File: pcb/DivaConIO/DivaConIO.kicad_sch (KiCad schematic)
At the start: 59 parts, among them J1 Conn_01x06_MountingPin, J2 Conn_01x04_MountingPin, J3 Conn_01x06_MountingPin, J4 Conn_01x08_MountingPin, J5 JST_SH_BM03B-SRSS-TB, J6 Conn_01x05_MountingPin, J7 Conn_01x06_MountingPin, Q1 BSS138, Q2 BSS138, Q3 BSS138, Q4 BSS138, Q5 BSS138, SW1 SW_Push

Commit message: revision 1.0 pcb schematics and layout
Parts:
- removed C5, C6: 1u0, Capacitor_SMD:C_0603_1608Metric, symbol Device:C_Small
- removed Q1: BSS138, Package_TO_SOT_SMD:SOT-23, symbol Transistor_FET:BSS138
- added C7: 100n, Capacitor_SMD:C_0603_1608Metric, symbol Device:C_Small
- added FID1, FID2, FID3, FID4: Fiducial, Fiducial:Fiducial_0.5mm_Mask1.5mm, symbol Mechanical:Fiducial
- added TP1, TP10, TP11, TP12, TP2, TP3, TP4, TP5, TP6, TP7, TP8, TP9: TestPoint, TestPoint:TestPoint_Pad_D2.0mm, symbol Connector:TestPoint
- added U1: 74HCT1G14, Package_TO_SOT_SMD:SC-74A-5_1.55x2.9mm_P0.95mm, symbol 74xGxx:74AHCT1G14
- J1, J3, J7: value Conn_01x06_MountingPin -> B6B-PH-SM4-TBT
- J2: value Conn_01x04_MountingPin -> B4B-PH-SM4-TBT
- J4: value Conn_01x08_MountingPin -> B8B-PH-SM4-TBT
- J5: value JST_SH_BM03B-SRSS-TB -> BM03B-SRSS-TBT
- R18: value 4K7 -> 330R
- R19: value 10R -> 10K
- SW1: footprint Button_Switch_SMD:SW_Push_SPST_NO_Alps_SKRK -> DivaConIO:SW_Push_SPST_NO_Alps_SKRP
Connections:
- net +3V3: now also TP1.1
- net +5V: now also C7.1, TP2.1, U1.5 (VCC); no longer R18.1
- net Display_I2C0_SCL: now also TP8.1
- net Display_I2C0_SDA: now also TP7.1
- net GND: now also R19.2, C7.2, TP10.1, TP4.1, U1.3 (GND)
- net Slider_I2C1_SCL: now also R13.2, TP5.1; no longer R15.2
- net Slider_I2C1_SDA: now also J4.4 (Pin_4), R15.2, TP6.1; no longer J4.6 (Pin_6), R13.2
- net Slider_LED_Data: now also U1.2
- net at R18.2: now also J4.6 (Pin_6), TP3.1; no longer J4.4 (Pin_4)
- net at J5.1 (Pin_1): now also A1.D1 (SWCLK), TP11.1; no longer A1.D3 (SWDIO)
- net at J5.3 (Pin_3): now also A1.D3 (SWDIO), TP12.1; no longer A1.D1 (SWCLK)
- net at A1.30 (RUN), R20.2, SW1.2: now also TP9.1
- net LED_Circle renamed LED-_Circle
- net LED_Cross renamed LED-_Cross
- net LED_Square renamed LED-_Square
- net LED_Triangle renamed LED-_Triangle
- new net: R18.1, U1.4
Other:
- moved on the sheet: J4, J5, R13, R15, R16, R17, R20, SW1

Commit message: revision 1.1 pcb schematics and layout
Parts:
- removed R23: 10R, Resistor_SMD:R_0603_1608Metric, symbol Device:R
- removed R26: 330R, Resistor_SMD:R_0603_1608Metric, symbol Device:R
- added R20: 10R, Resistor_SMD:R_0603_1608Metric, symbol Device:R
- added R32: 330R, Resistor_SMD:R_0603_1608Metric, symbol Device:R
- renumbered C7 to C5, FID3 to FID2, FID2 to FID3, J6 to J4, J4 to J6, Q5 to Q1, Q4 to Q2, Q2 to Q4, R9 to R10, R31 to R11, R10 to R12, R30 to R13, R11 to R14, R29 to R15, R12 to R16, R14 to R17, R20 to R18, R24 to R19, R19 to R23, R28 to R24, R18 to R26, R17 to R28, R16 to R29, R15 to R30, R13 to R31, R32 to R9, TP12 to TP1, TP5 to TP10, TP3 to TP11, TP10 to TP12, TP11 to TP2, TP9 to TP3, TP2 to TP4, TP4 to TP5, TP1 to TP6, TP8 to TP7, TP7 to TP8, TP6 to TP9
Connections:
- net +3V3: now also J6.5 (Pin_5), TP5.1; no longer J6.7 (Pin_7), TP6.1
- net +5V: now also J6.7 (Pin_7), J7.1 (Pin_1), J7.2 (Pin_2); no longer J6.8 (Pin_8), J7.5 (Pin_5), J7.6 (Pin_6)
- net Button_Circle: now also A1.17 (GPIO13), J4.5 (Pin_5); no longer A1.27 (GPIO21), J4.2 (Pin_2)
- net Button_Cross: now also A1.19 (GPIO14), J4.4 (Pin_4); no longer A1.26 (GPIO20), J4.3 (Pin_3)
- net Button_Square: now also A1.20 (GPIO15), J4.3 (Pin_3); no longer A1.25 (GPIO19), J4.4 (Pin_4)
- net Button_Triangle: now also A1.21 (GPIO16), J4.2 (Pin_2); no longer A1.24 (GPIO18), J4.5 (Pin_5)
- net Display_I2C0_SCL: now also A1.27 (GPIO21), J6.1 (Pin_1), R31.2, TP11.1; no longer A1.22 (GPIO17), J6.2 (Pin_2), R28.2, TP7.1
- net Display_I2C0_SDA: now also A1.26 (GPIO20), J6.2 (Pin_2), R30.2, TP10.1; no longer A1.21 (GPIO16), J6.3 (Pin_3), R29.2, TP8.1
- net GND: now also J6.6 (Pin_6), TP6.1; no longer J6.1 (Pin_1), TP5.1
- net LED-_Circle: now also J7.6 (Pin_6), R32.1; no longer J7.1 (Pin_1), R24.1
- net LED-_Cross: now also J7.5 (Pin_5); no longer J7.2 (Pin_2)
- net LED-_Square: now also J7.4 (Pin_4), R25.1; no longer J7.3 (Pin_3)
- net LED-_Triangle: now also J7.3 (Pin_3), R24.1; no longer J7.4 (Pin_4), R25.1
- net LED_En_Circle: now also A1.29 (GPIO22), R22.1; no longer A1.34 (GPIO28_ADC2), R19.1
- net LED_En_Cross: now also A1.31 (GPIO26_ADC0), R21.1; no longer A1.32 (GPIO27_ADC1)
- net LED_En_Square: now also A1.32 (GPIO27_ADC1), R20.1; no longer A1.31 (GPIO26_ADC0), R22.1
- net LED_En_Triangle: now also A1.34 (GPIO28_ADC2), R19.1; no longer A1.29 (GPIO22), R21.1
- net Slider_I2C1_SCL: now also A1.25 (GPIO19), J6.3 (Pin_3), R29.2, TP9.1; no longer A1.20 (GPIO15), J6.5 (Pin_5), R31.2, TP10.1
- net Slider_I2C1_SDA: now also A1.24 (GPIO18), R28.2, TP8.1; no longer A1.19 (GPIO14), R30.2, TP9.1
- net Slider_LED_Data: now also A1.22 (GPIO17); no longer A1.17 (GPIO13)
- net at Q2.1 (G): now also R20.2
- net at Q2.3 (D): now also R25.2; no longer R27.2
- net at R22.2: now also Q4.1 (G); no longer Q3.1 (G)
- net at Q3.3 (D): now also R27.2
- net at R21.2: now also Q3.1 (G); no longer Q4.1 (G)
- net at Q4.3 (D): now also R32.2; no longer R25.2
- net at A1.D1 (SWCLK), J5.1 (Pin_1): now also TP1.1; no longer TP2.1
- net at A1.D3 (SWDIO), J5.3 (Pin_3): now also TP2.1; no longer TP1.1
- new net: J6.8 (Pin_8), R26.2, TP7.1
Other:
- moved on the sheet: A1, C1, C2, C3, C4, C5, FID1, FID2, FID3, FID4, H1, H2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

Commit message: Update PCBs to purchased revision
Main edit is using a ULN2003 NPN transistor array over discrete MOSFETs.
This was chosen because there was limited board space to put in
pull-down resistors on the board and it was complicating the single
layer routing. The PCB had to be expanded to 70x75mm anyways to
accommodate the SOIC ic anyways.

The schematics of the IO board were also updated to use net labels over
direct wiring. Due to the JST connectors and the Pi Pico schematic
symbol being mirrored, it was getting too difficult to have an
understandable schematic.

Minor edit was changing LED_DATA to nLED_DATA to signify that it is
an active low signal.
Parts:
- removed Q1, Q2, Q3, Q4: BSS138, Package_TO_SOT_SMD:SOT-23, symbol Transistor_FET:BSS138
- removed R19, R20: 10R, Resistor_SMD:R_0603_1608Metric, symbol Device:R
- removed R25, R27, R32: 330R, Resistor_SMD:R_0603_1608Metric, symbol Device:R
- added R23: 270R, Resistor_SMD:R_1206_3216Metric, symbol Device:R
- added U2: ULN2003D1013TR, Package_SO:SOIC-16_3.9x9.9mm_P1.27mm, symbol Transistor_Array:ULN2003
- A1: Manufacturer (none) -> Raspberry Pi; PartNumber (none) -> SC0915
- C1, C3: Dielectric (none) -> X7R; Manufacturer (none) -> Samsung Electro-Mechanical; PartNumber (none) -> CL10B105KO8NNNC; Voltage (none) -> 16V
- C2, C4, C5: Dielectric (none) -> X7R; Manufacturer (none) -> Samsung Electro-Mechanical; PartNumber (none) -> CL10B104KB8NNNC; Voltage (none) -> 50V
- H1, H2, H3, H4: value MountingHole_Pad -> Standoff_M3; now in the parts list
- J1, J3: Manufacturer (none) -> JST; PartNumber (none) -> B6B-PH-SM4-TBT
- J2: Manufacturer (none) -> JST; PartNumber (none) -> B4B-PH-SM4-TBT
- J4: value Conn_01x05_MountingPin -> B5B-PH-SM4-TBT; Manufacturer (none) -> JST; PartNumber (none) -> B5B-PH-SM4-TBT
- J5: renamed from J6; Manufacturer (none) -> JST; PartNumber (none) -> B8B-PH-SM4-TBT
- J6: renamed from J7; Manufacturer (none) -> JST; PartNumber (none) -> B6B-PH-SM4-TBT
- J7: renamed from J5; Manufacturer (none) -> JST; PartNumber (none) -> BM03B-SRSS-TBT
- R1: renamed from R28; Manufacturer (none) -> Stackpole Electronics; PartNumber (none) -> RMCF0603FT4K70
- R10: renamed from R5; Manufacturer (none) -> Stackpole Electronics; PartNumber (none) -> RMCF0603FT10K0
- R11: renamed from R6; Manufacturer (none) -> Stackpole Electronics; PartNumber (none) -> RMCF0603FT10K0
- R12: renamed from R7; Manufacturer (none) -> Stackpole Electronics; PartNumber (none) -> RMCF0603FT10K0
- R13: renamed from R8; Manufacturer (none) -> Stackpole Electronics; PartNumber (none) -> RMCF0603FT10K0
- R14: renamed from R10; Manufacturer (none) -> Stackpole Electronics; PartNumber (none) -> RMCF0603FT10K0
- R15: renamed from R12; Manufacturer (none) -> Stackpole Electronics; PartNumber (none) -> RMCF0603FT10K0
- R16: renamed from R14; Manufacturer (none) -> Stackpole Electronics; PartNumber (none) -> RMCF0603FT10K0
- R17: renamed from R16; Manufacturer (none) -> Stackpole Electronics; PartNumber (none) -> RMCF0603FT10K0
- R18: renamed from R17; Manufacturer (none) -> Stackpole Electronics; PartNumber (none) -> RMCF0603FT10K0
- R19: renamed from R26; value 330R -> 470R; Manufacturer (none) -> Stackpole Electronics; PartNumber (none) -> RMCF0603FT470R
- R2: renamed from R29; Manufacturer (none) -> Stackpole Electronics; PartNumber (none) -> RMCF0603FT4K70
- R20: renamed from R23; Manufacturer (none) -> Stackpole Electronics; PartNumber (none) -> RMCF0603FT10K0
- R21, R22: value 10R -> 270R; footprint Resistor_SMD:R_0603_1608Metric -> Resistor_SMD:R_1206_3216Metric; Manufacturer (none) -> Stackpole Electronics; PartNumber (none) -> RMCF1206JT270R
- R24: value 330R -> 270R; footprint Resistor_SMD:R_0603_1608Metric -> Resistor_SMD:R_1206_3216Metric; Manufacturer (none) -> Stackpole Electronics; PartNumber (none) -> RMCF1206JT270R
- R26: renamed from R15; Manufacturer (none) -> Stackpole Electronics; PartNumber (none) -> RMCF0603FT10K0
- R27: renamed from R13; Manufacturer (none) -> Stackpole Electronics; PartNumber (none) -> RMCF0603FT10K0
- R28: renamed from R11; Manufacturer (none) -> Stackpole Electronics; PartNumber (none) -> RMCF0603FT10K0
- R29: renamed from R9; Manufacturer (none) -> Stackpole Electronics; PartNumber (none) -> RMCF0603FT10K0
- R3: renamed from R30; Manufacturer (none) -> Stackpole Electronics; PartNumber (none) -> RMCF0603FT4K70
- R4: renamed from R31; Manufacturer (none) -> Stackpole Electronics; PartNumber (none) -> RMCF0603FT4K70
- R5: renamed from R18; Manufacturer (none) -> Stackpole Electronics; PartNumber (none) -> RMCF0603FT10K0
- R6: renamed from R1; Manufacturer (none) -> Stackpole Electronics; PartNumber (none) -> RMCF0603FT10K0
- R7: renamed from R2; Manufacturer (none) -> Stackpole Electronics; PartNumber (none) -> RMCF0603FT10K0
- R8: renamed from R3; Manufacturer (none) -> Stackpole Electronics; PartNumber (none) -> RMCF0603FT10K0
- R9: renamed from R4; Manufacturer (none) -> Stackpole Electronics; PartNumber (none) -> RMCF0603FT10K0
- SW1: value SW_Push -> SKRPABE010; Manufacturer (none) -> Alps Alpine; PartNumber (none) -> SKRPABE010
- TP1, TP2, TP8: now left out of the parts list
- TP10: renamed from TP3; now left out of the parts list
- TP11: renamed from TP12; now left out of the parts list
- TP12: renamed from TP6; now left out of the parts list
- TP3: renamed from TP4; now left out of the parts list
- TP4: renamed from TP5; now left out of the parts list
- TP5: renamed from TP7; now left out of the parts list
- TP6: renamed from TP9; now left out of the parts list
- TP7: renamed from TP11; now left out of the parts list
- TP9: renamed from TP10; now left out of the parts list
- U1: value 74HCT1G14 -> 74HCT1G14GV,125; Manufacturer (none) -> Nexperia; PartNumber (none) -> 74HCT1G14GV,125
- renumbered FID3 to FID2, FID2 to FID3
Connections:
- net Button_Down: now also A1.16 (GPIO12), J3.2 (Pin_2), R18.2; no longer A1.11 (GPIO8), J3.6 (Pin_6), R14.2
- net Button_Home: now also A1.9 (GPIO6), J2.3 (Pin_3), R12.2; no longer A1.10 (GPIO7), J2.2 (Pin_2), R13.2
- net Button_L2: now also A1.12 (GPIO9), J3.5 (Pin_5), R15.2; no longer A1.15 (GPIO11), J3.3 (Pin_3), R17.2
- net Button_L3: now also A1.11 (GPIO8), J3.6 (Pin_6), R14.2; no longer A1.16 (GPIO12), J3.2 (Pin_2), R18.2
- net Button_Left: now also A1.6 (GPIO4), J1.2 (Pin_2), R10.2; no longer A1.1 (GPIO0), J1.6 (Pin_6), R6.2
- net Button_R1: now also A1.4 (GPIO2), J1.4 (Pin_4), R8.2; no longer A1.6 (GPIO4), J1.2 (Pin_2), R10.2
- net Button_R2: now also A1.2 (GPIO1), J1.5 (Pin_5), R7.2; no longer A1.5 (GPIO3), J1.3 (Pin_3), R9.2
- net Button_R3: now also A1.1 (GPIO0), J1.6 (Pin_6), R6.2; no longer A1.4 (GPIO2), J1.4 (Pin_4), R8.2
- net Button_Right: now also A1.5 (GPIO3), J1.3 (Pin_3), R9.2; no longer A1.2 (GPIO1), J1.5 (Pin_5), R7.2
- net Button_Start: now also A1.10 (GPIO7), J2.2 (Pin_2), R13.2; no longer A1.9 (GPIO6), J2.3 (Pin_3), R12.2
- net Button_Up: now also A1.15 (GPIO11), J3.3 (Pin_3), R17.2; no longer A1.12 (GPIO9), J3.5 (Pin_5), R15.2
- net GND: now also U2.2 (I2), U2.4 (I4), U2.6 (I6), U2.8 (GND)
- net LED-_Circle: now also R24.2
- net LED-_Cross: now also R23.2
- net LED-_Square: now also R22.2
- net LED-_Triangle: now also R21.2; no longer R24.1
- net LED_En_Circle: now also U2.7 (I7); no longer R22.1
- net LED_En_Cross: now also U2.5 (I5); no longer R21.1
- net LED_En_Square: now also U2.3 (I3)
- net LED_En_Triangle: now also U2.1 (I1)
- net nSlider_LED_Data: now reaches J5.8 (Pin_8), R19.2, TP5.1
- new net: R21.1, U2.16 (O1)
- new net: R24.1, U2.10 (O7)
- new net: R23.1, U2.12 (O5)
- new net: R22.1, U2.14 (O3)
- no-connect marks 2 -> 6
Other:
- note added: "+5V"
- moved on the sheet: C1, C4, C5, FID1, FID2, FID3, FID4, H1, H2, H3, H4, J1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

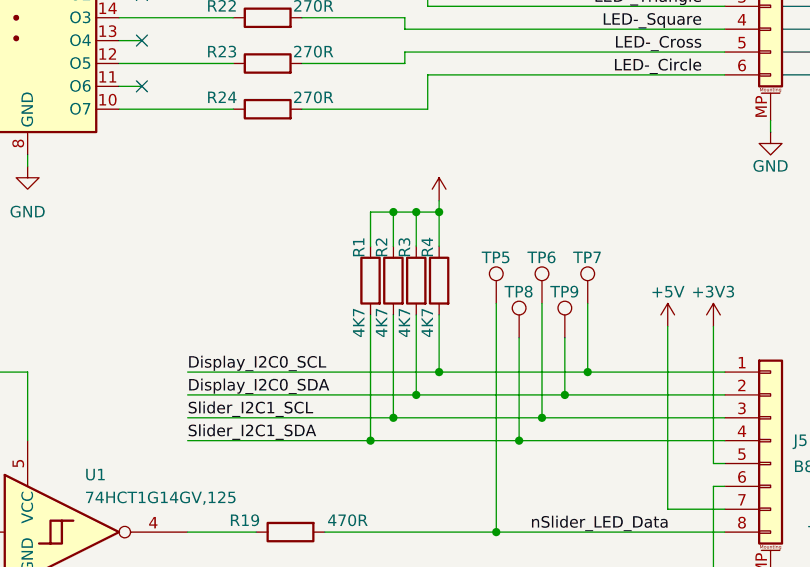
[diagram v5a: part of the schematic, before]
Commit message: Generate slider PCB 3d model
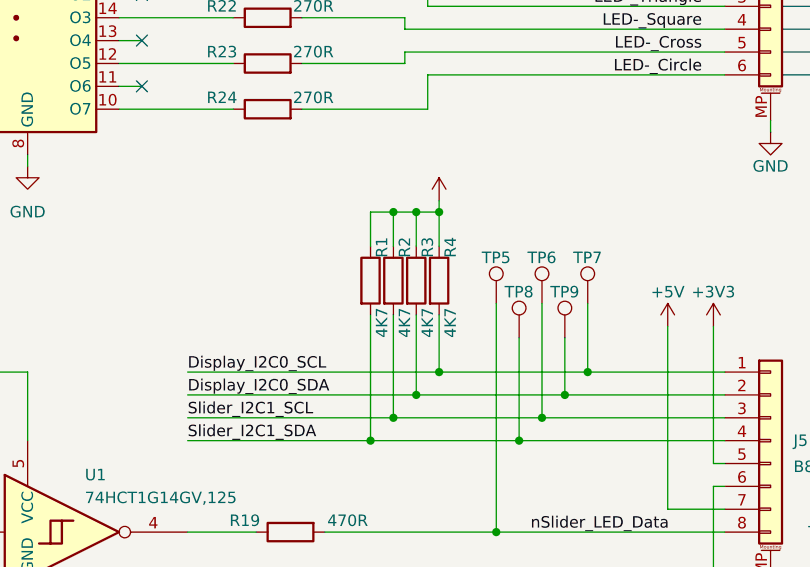
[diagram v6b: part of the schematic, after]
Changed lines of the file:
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@@
 		(lib_id "Device:R")
 		(at 331.47 119.38 0)
-		(mirror y)
 		(unit 1)
 		(exclude_from_sim no)
@@
 		(dnp no)
 		(property "Reference" "R4"
-			(at 330.2 116.84 90)
+			(at 332.74 116.84 90)
 			(effects
 				(font
@@
 		)
 		(property "Value" "4K7"
-			(at 330.2 125.73 90)
+			(at 332.74 125.73 90)
 			(effects
 				(font
@@
 		)
 		(property "Footprint" "Resistor_SMD:R_0603_1608Metric"
-			(at 333.248 119.38 90)
+			(at 329.692 119.38 90)
 			(effects
 				(font
@@
 		(lib_id "Device:R")
 		(at 323.85 119.38 0)
-		(mirror y)
 		(unit 1)
 		(exclude_from_sim no)
@@
 		(dnp no)
 		(property "Reference" "R1"
-			(at 322.58 116.84 90)
+			(at 325.12 116.84 90)
 			(effects
 				(font
@@
 		)
 		(property "Value" "4K7"
-			(at 322.58 125.73 90)
+			(at 325.12 125.73 90)
 			(effects
 				(font
@@
 		)
 		(property "Footprint" "Resistor_SMD:R_0603_1608Metric"
-			(at 325.628 119.38 90)
+			(at 322.072 119.38 90)
 			(effects
 				(font
@@
 		(lib_id "Device:R")
 		(at 326.39 119.38 0)
-		(mirror y)
 		(unit 1)
 		(exclude_from_sim no)
@@
 		(dnp no)
 		(property "Reference" "R2"
-			(at 325.12 116.84 90)
+			(at 327.66 116.84 90)
 			(effects
 				(font
@@
 		)
 		(property "Value" "4K7"
-			(at 325.12 125.73 90)
+			(at 327.66 125.73 90)
 			(effects
 				(font
@@
 		)
 		(property "Footprint" "Resistor_SMD:R_0603_1608Metric"
-			(at 328.168 119.38 90)
+			(at 324.612 119.38 90)
 			(effects
 				(font
@@
 		(lib_id "Device:R")
 		(at 328.93 119.38 0)
-		(mirror y)
 		(unit 1)
 		(exclude_from_sim no)
@@
 		(dnp no)
 		(property "Reference" "R3"
-			(at 327.66 116.84 90)
+			(at 330.2 116.84 90)
 			(effects
 				(font
@@
 		)
 		(property "Value" "4K7"
-			(at 327.66 125.73 90)
+			(at 330.2 125.73 90)
 			(effects
 				(font
@@
 		)
 		(property "Footprint" "Resistor_SMD:R_0603_1608Metric"
-			(at 330.708 119.38 90)
-			(effects
-				(font
+			(at 327.152 119.38 90)
+			(effects
+				(font
